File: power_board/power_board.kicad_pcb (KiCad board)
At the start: 4 copper layers, 60 x 46 mm, 53 parts, among them J1 USB-C receptacle (input from 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, J2 USB-C receptacle (5 V to Pi), J3 Lidar 15 V (pluggable 3.5 mm), J4 Latching 16 mm LED button (JS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, J5 To Pi GPIO (JST-PH 10), U1 CH224A, U3 TPS56637RPA, U4 TPS26631PWP, U5 INA226 (addr 0x40)

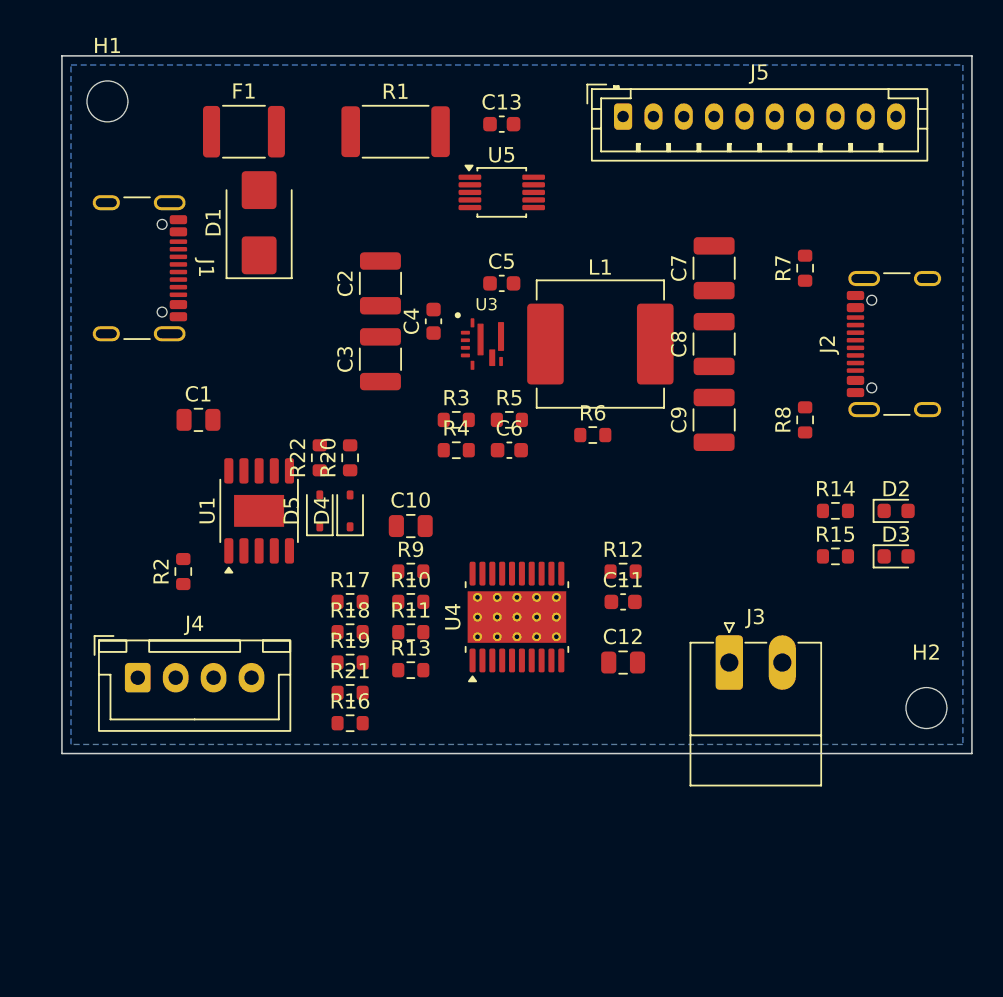
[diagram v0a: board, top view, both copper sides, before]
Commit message: Power board: TPS56637 RPA0010A footprint from the datasheet land pattern, upright 46x60 board for the buck bay, USB-C on the top edge, top-entry lidar terminal, button LED from the switch
Co-Authored-By: Claude Opus 5.5 <noreply@anthropic.com>
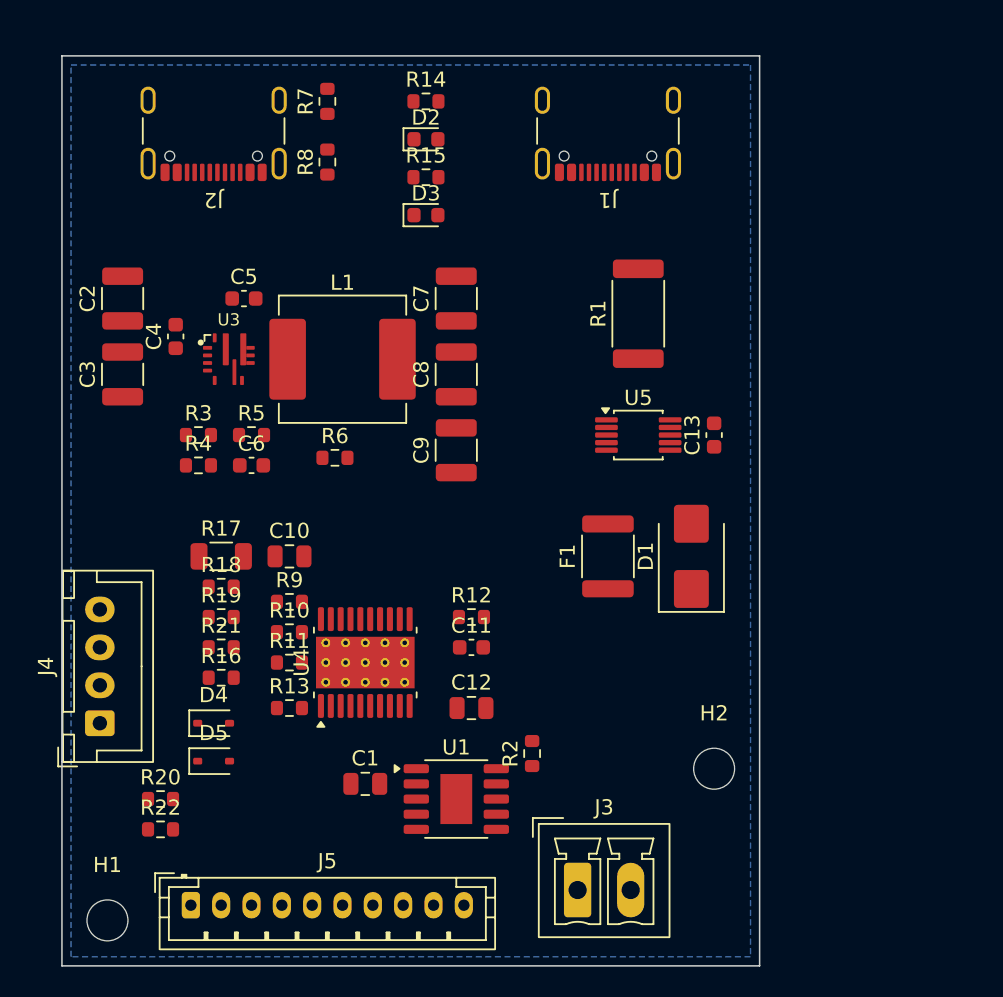
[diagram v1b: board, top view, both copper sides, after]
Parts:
- J3: footprint Connector_Phoenix_MC:PhoenixContact_MC_1,5_2-G-3.5_1x02_P3.50mm_Horizontal -> Connector_Phoenix_MC:PhoenixContact_MCV_1,5_2-G-3.5_1x02_P3.50mm_Vertical
- R17: value 1k -> 100R 1206; footprint Resistor_SMD:R_0603_1608Metric -> Resistor_SMD:R_1206_3216Metric
- U3: footprint power_board:TI_RPA0010A_PLACEHOLDER -> power_board:TI_RPA0010A
- moved J5 59.3 mm to (8.50, 56.0)
- moved H1 54.0 mm to (3.00, 57.0)
- moved J2 48.4 mm to (10.0, 4.00), turned to 180 degrees
- moved D2 39.5 mm to (24.0, 5.50)
- moved D3 38.3 mm to (24.0, 10.5)
- moved R14 38.2 mm to (24.0, 3.00)
- moved F1 36.9 mm to (36.0, 33.0), turned to 90 degrees
- moved R15 36.8 mm to (24.0, 8.00)
- moved D1 36.0 mm to (41.5, 33.0)
- moved R8 35.8 mm to (17.5, 7.00)
- moved J1 33.5 mm to (36.0, 4.00), turned to 180 degrees
- moved R7 33.4 mm to (17.5, 3.00)
- moved R22 26.7 mm to (6.50, 51.0), turned to 0 degrees
- moved C1 26.4 mm to (20.0, 48.0)
- moved R2 25.9 mm to (31.0, 46.0)
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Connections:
- R16 pad 1: /V5 -> /SW_ON
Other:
- board size 60 x 46 mm -> 46 x 60 mm

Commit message: Power board: TI RPA0010A footprint (Ultra Librarian, fingers fixed to pad 8), buck placed per datasheet layout guide, input chain in signal order
Co-Authored-By: Claude Opus 5.5 <noreply@anthropic.com>
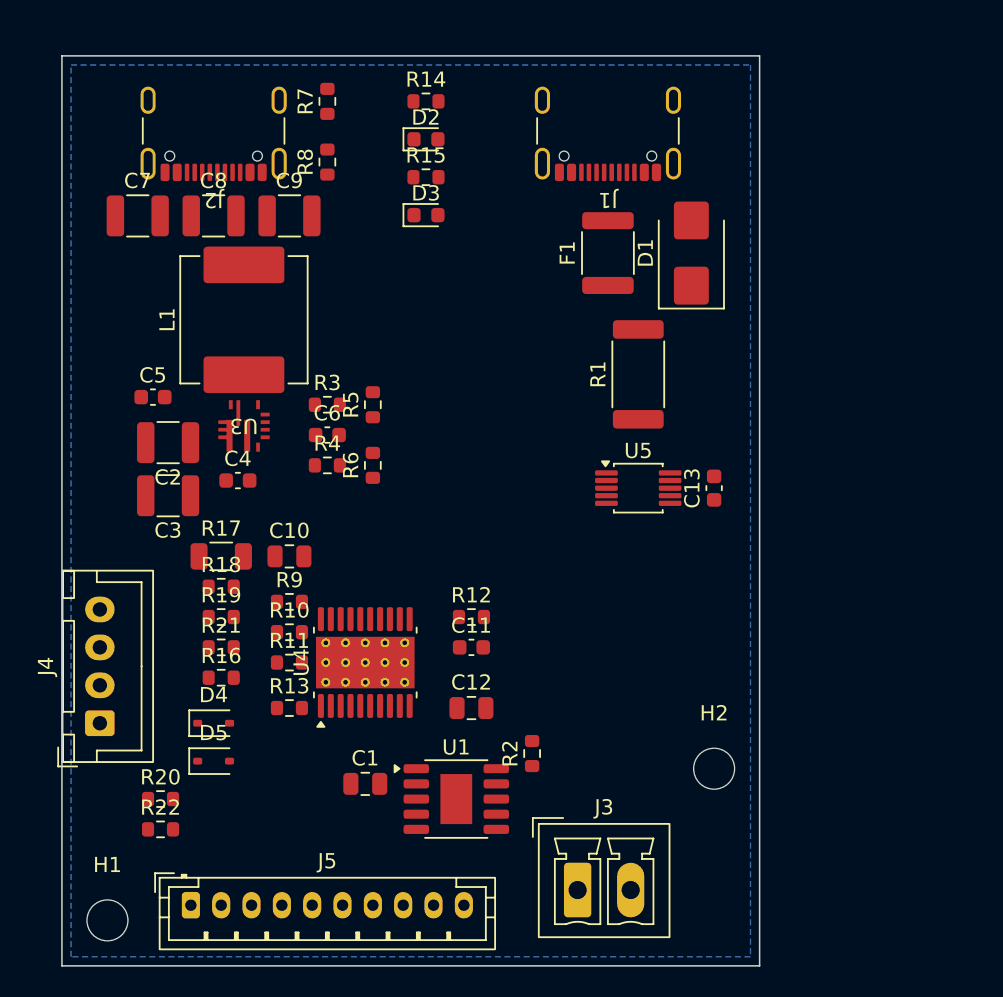
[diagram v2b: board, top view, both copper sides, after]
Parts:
- U3: footprint power_board:TI_RPA0010A -> power_board:RPA0010A
- moved C7 21.7 mm to (5.00, 10.6), turned to 0 degrees
- moved D1 20.0 mm to (41.5, 13.0)
- moved F1 20.0 mm to (36.0, 13.0)
- moved C8 19.1 mm to (10.0, 10.6), turned to 0 degrees
- moved C9 19.0 mm to (15.0, 10.6), turned to 0 degrees
- moved C4 10.3 mm to (11.6, 28.0), turned to 0 degrees
- moved C2 9.96 mm to (7.00, 25.5), turned to 180 degrees
- moved C5 8.85 mm to (6.00, 22.5)
- moved R3 8.73 mm to (17.5, 23.0)
- moved C3 8.54 mm to (7.00, 29.0), turned to 180 degrees
- moved R4 8.50 mm to (17.5, 27.0)
- moved R5 8.25 mm to (20.5, 23.0), turned to 90 degrees
- moved L1 7.00 mm to (12.0, 17.4), turned to 90 degrees
- moved C6 5.39 mm to (17.5, 25.0)
- moved U3 4.51 mm to (12.0, 24.4), turned to 180 degrees
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
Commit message: Power board: route the buck (VIN/PGND pours under the chip, SW stub, boot cap, V5 pour to J2, FB column with separate V5 sense on In2, AGND via, EN/PG escapes), J2 CC pull-ups
Co-Authored-By: Claude Opus 5.5 <noreply@anthropic.com>
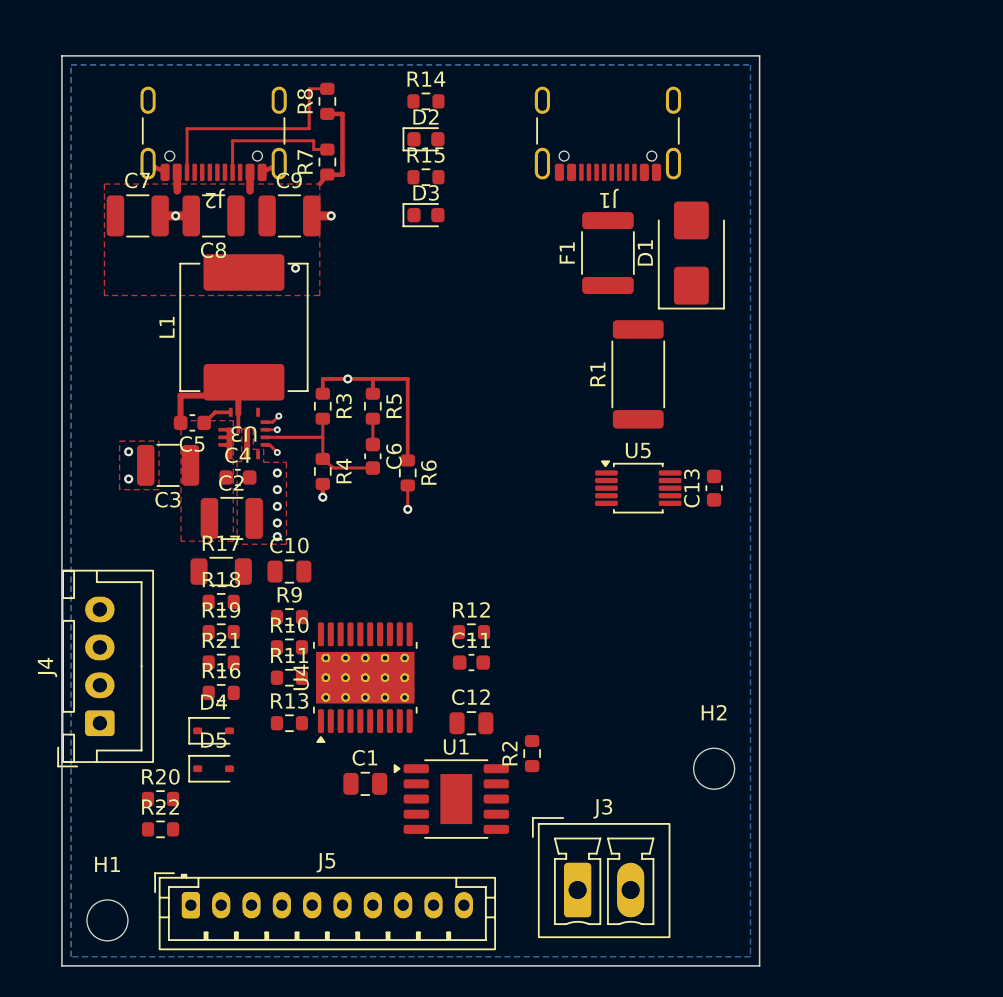
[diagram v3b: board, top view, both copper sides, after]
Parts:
- moved C2 6.53 mm to (11.2, 30.5), turned to 0 degrees
- moved R7 4.00 mm to (17.5, 7.00)
- moved R8 4.00 mm to (17.5, 3.00)
- moved C6 3.31 mm to (20.5, 26.4), turned to -90 degrees
- moved C5 3.11 mm to (8.60, 24.2), turned to 180 degrees
- moved R6 2.35 mm to (22.8, 27.5), turned to -90 degrees
- moved C3 2.00 mm to (7.00, 27.0)
- moved C10 1.00 mm to (15.0, 34.0)
- moved C11 1.00 mm to (27.0, 40.0)
- moved C12 1.00 mm to (27.0, 44.0)
- moved R10 1.00 mm to (15.0, 39.0)
- moved R11 1.00 mm to (15.0, 41.0)
- moved R12 1.00 mm to (27.0, 38.0)
- moved R13 1.00 mm to (15.0, 44.0)
- moved R16 1.00 mm to (10.5, 42.0)
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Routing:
- net /V5: track 0.00 -> 32.9 mm, vias 0 -> 2
- net /BUCK_PG: track 0.00 -> 17.3 mm, vias 0 -> 2
- net /OUT_CC2: track 0.00 -> 14.8 mm
- net /BUCK_FB: track 0.00 -> 9.96 mm
- net /OUT_CC1: track 0.00 -> 8.90 mm
- net /GND: track 0.00 -> 7.51 mm, vias 0 -> 11
- net /BUCK_SW: track 0.00 -> 4.78 mm
- net /BUCK_BOOT: track 0.00 -> 2.03 mm
- net /BUCK_FF: track 0.00 -> 1.70 mm
- net /BUCK_EN: track 0.00 -> 1.01 mm, vias 0 -> 1
- added copper zone on F.Cu, net /GND
- added copper zone on F.Cu, net /V15
- added copper zone on F.Cu, net /V5

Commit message: Power board: fully routed (hand-routed power + Kelvin sense, In1 GND / In2 V15 planes, fan-out vias, Freerouting for signals), DRC clean; build_all.ps1 and export_fab.ps1
Co-Authored-By: Claude Opus 5.5 <noreply@anthropic.com>
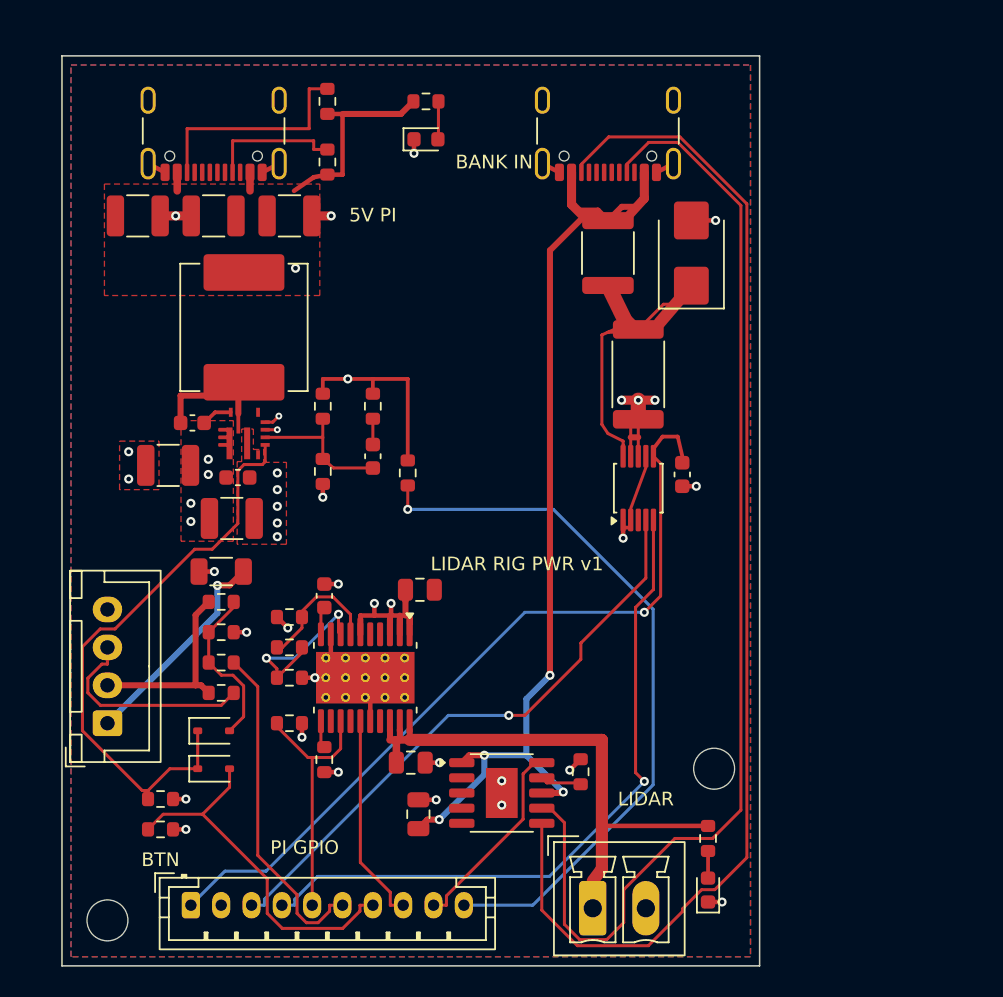
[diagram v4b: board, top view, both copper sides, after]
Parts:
- moved D3 48.2 mm to (42.6, 55.0), turned to 90 degrees
- moved R15 47.4 mm to (42.6, 51.6), turned to -90 degrees
- moved R12 12.8 mm to (17.3, 46.4), turned to -90 degrees
- moved C11 10.7 mm to (17.3, 35.6), turned to 90 degrees
- moved C10 8.68 mm to (23.6, 35.2)
- moved C12 4.77 mm to (23.0, 46.6)
- moved C1 4.03 mm to (23.5, 50.0), turned to 90 degrees
- moved R2 3.42 mm to (34.2, 47.2)
- moved U1 3.03 mm to (29.0, 48.6)
- moved C13 2.28 mm to (40.9, 27.6), turned to -90 degrees
- moved J3 1.56 mm to (35.0, 56.2)
- moved J4 0.50 mm to (3.00, 44.0)
- turned F1 to -90 degrees
- turned R1 to -90 degrees
- turned U4 to -90 degrees
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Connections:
- J1 pad A6: /IN_DP -> unconnected-(J1-D+-PadA6)
- J1 pad A7: /IN_DM -> unconnected-(J1-D--PadA7)
- J1 pad B6: /IN_DP -> unconnected-(J1-D+-PadB6)
- J1 pad B7: /IN_DM -> unconnected-(J1-D--PadB7)
- U1 pad 4: /IN_DP -> unconnected-(U1-DP-Pad4)
- U1 pad 5: /IN_DM -> unconnected-(U1-DM-Pad5)
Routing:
- net /IN_CC2: track 0.00 -> 79.9 mm
- net /IN_CC1: track 0.00 -> 75.7 mm
- net /VBUS_RAW: track 0.00 -> 64.4 mm, vias 0 -> 4
- net /3V3_PI: track 0.00 -> 53.1 mm, vias 0 -> 1
- net /BUCK_PG: track 17.3 -> 63.5 mm
- net /SCL: track 0.00 -> 45.5 mm, vias 0 -> 1
- net /SDA: track 0.00 -> 39.6 mm, vias 0 -> 1
- net /BUCK_EN: track 1.01 -> 38.7 mm, vias 1 -> 0
- net /VLIDAR: track 0.00 -> 37.5 mm
- net /KEEP_ALIVE: track 0.00 -> 24.3 mm
- net /VIN15: track 0.00 -> 22.4 mm
- net /SW_SENSE: track 0.00 -> 22.2 mm
- net /GND: track 7.51 -> 29.5 mm, vias 11 -> 28
- net /V15: track 0.00 -> 21.1 mm, vias 0 -> 11
- net /LIDAR_EN: track 0.00 -> 17.1 mm
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- added copper zone on In2.Cu, net /V15
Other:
- board text added: "5V PI"
- board text added: "BANK IN"
- board text added: "BTN"
- board text added: "LIDAR"
- board text added: "LIDAR RIG PWR v1"
- board text added: "PI GPIO"

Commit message: Power board: in-stock parts (MDA7050 inductor, 2920 PTC, Kefa terminal, uprated 1210 caps), D+/D- dropped, input sense block shifted for the fuse; DRC 0 violations; JLC BOM/CPL generator
Co-Authored-By: Claude Opus 5.5 <noreply@anthropic.com>
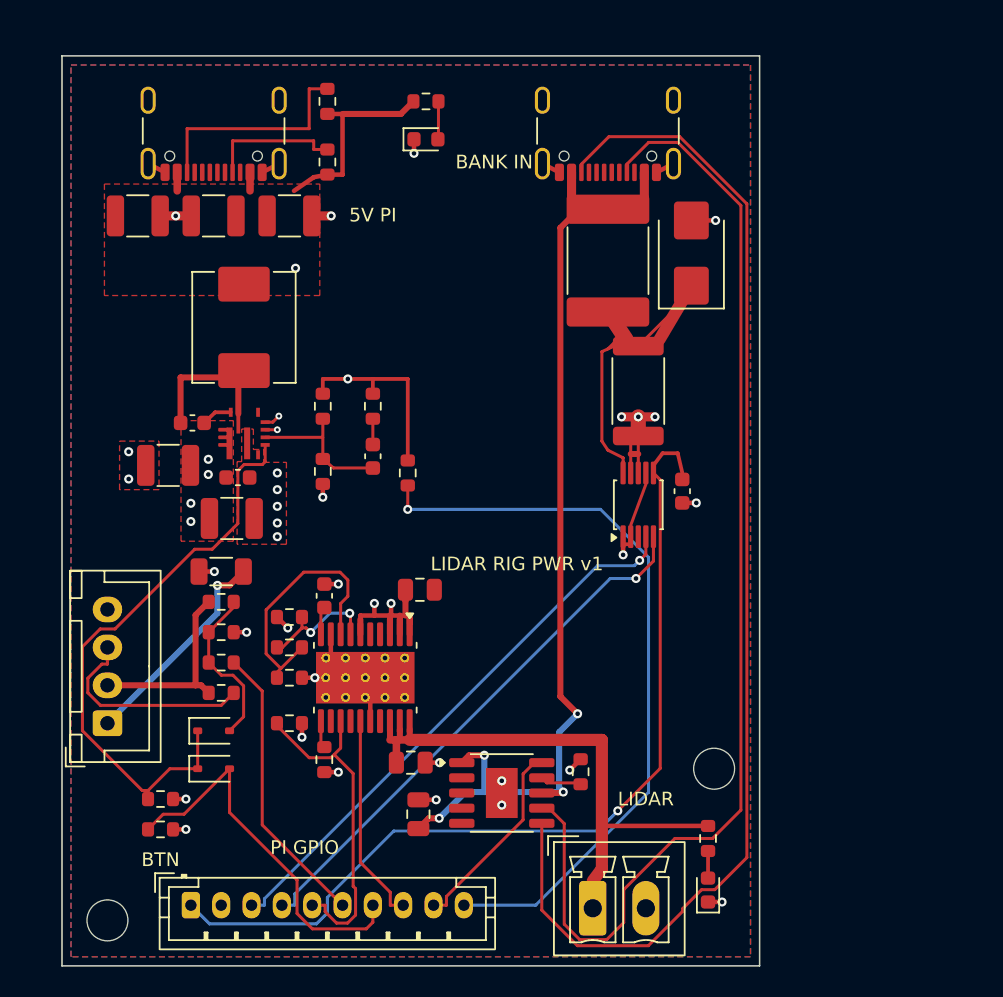
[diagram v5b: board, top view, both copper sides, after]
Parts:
- C2, C3: value 10u 35V -> 10u 50V
- C7, C8, C9: value 22u 16V -> 22u 25V
- F1: value 3A hold PTC -> 3A hold PTC 2920; footprint Fuse:Fuse_1812_4532Metric -> Fuse:Fuse_2920_7451Metric
- L1: value 3.3u Isat>=10A -> 3.3u MDA7050 9.5A; footprint Inductor_SMD:L_Vishay_IHLP-3232 -> Inductor_SMD:L_KOHERelec_MDA7030
- moved R1 1.10 mm to (38.0, 22.1)
- moved U5 1.10 mm to (38.0, 29.6)
- moved C13 1.10 mm to (40.9, 28.7)
- moved F1 0.50 mm to (36.0, 13.5)
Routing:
- net /SCL: track 45.5 -> 35.9 mm
- net /3V3_PI: track 53.1 -> 60.2 mm
- net /EF_OVP: track 11.6 -> 17.4 mm, vias 2 -> 0
- net /LIDAR_EN: track 17.1 -> 22.3 mm
- net /SW_SENSE: track 22.2 -> 19.0 mm
- net /SDA: track 39.6 -> 37.0 mm
- net /BUCK_SW: track 8.29 -> 10.4 mm
- net /VBUS_RAW: track 64.4 -> 66.3 mm
- net /BUCK_PG: track 63.5 -> 65.2 mm
- net /KEEP_ALIVE: track 24.3 -> 25.1 mm
- net /VLIDAR: track 37.5 -> 38.3 mm
- net /EF_UVLO: track 8.66 -> 8.04 mm, vias 0 -> 2

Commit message: Power board: small vias 0.45/0.3 (JLC standard tier, no high-precision surcharge), annular rule 0.075, router-only stub cleanup in its own process
Co-Authored-By: Claude Opus 5.5 <noreply@anthropic.com>
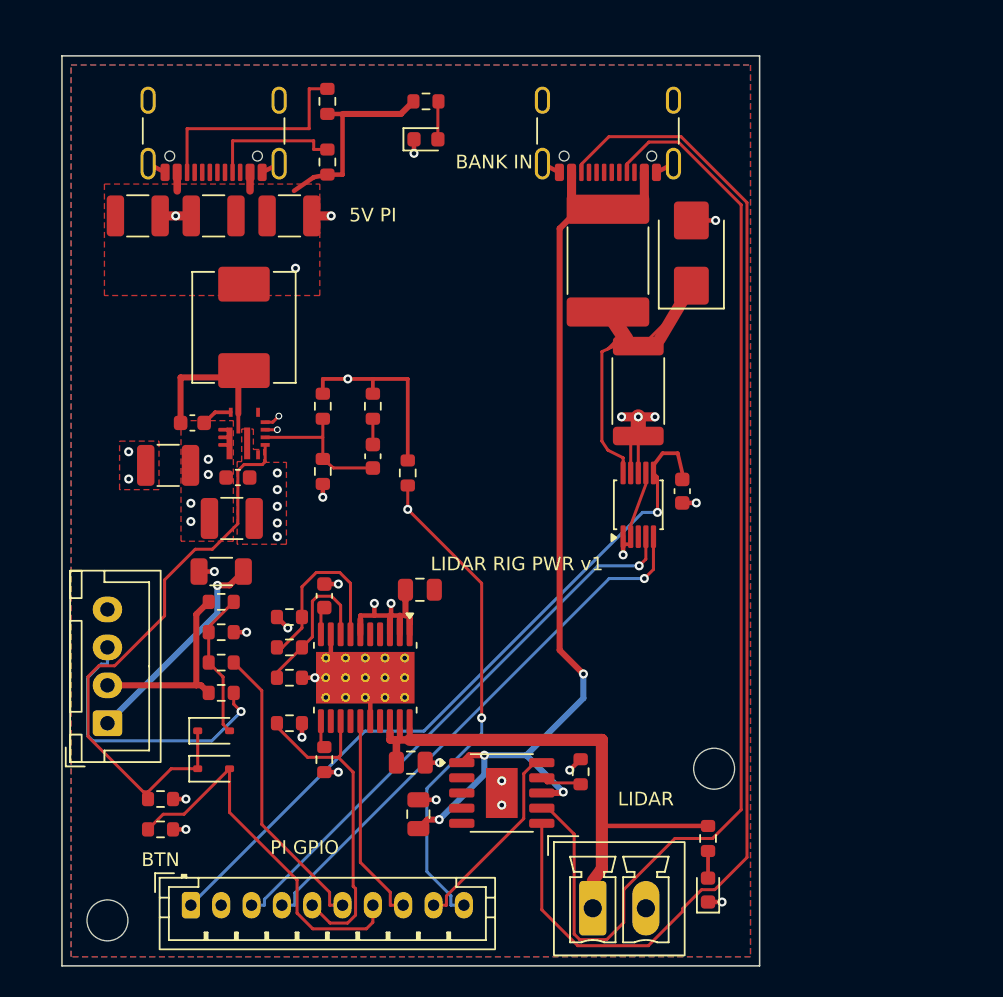
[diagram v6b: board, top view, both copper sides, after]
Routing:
- net /BUCK_PG: track 65.2 -> 48.4 mm, vias 2 -> 3
- net /3V3_PI: track 60.2 -> 48.5 mm
- net /EF_OVP: track 17.4 -> 10.2 mm
- net /BTN_LED_A: track 14.0 -> 19.1 mm, vias 0 -> 1
- net /EF_UVLO: track 8.04 -> 12.1 mm, vias 2 -> 0
- net /VIN15: track 22.7 -> 21.3 mm
- net /SW_TAP: track 11.0 -> 9.75 mm
- net /VBUS_RAW: track 66.3 -> 65.3 mm
- net /V15: track 21.1 -> 20.6 mm
